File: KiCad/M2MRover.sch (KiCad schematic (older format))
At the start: 39 parts, among them J1 Light Detection, J10 MPU6050 Gyro & Acc GY-521, J11 microbit_edge_connector, J2 Serial (Bluetooth), J3 Servo, J4 H-Bridge, J5 Ultrasonic Down, J6 Ultrasonic Forward, J7 Compass GY-273, J8 Left Hall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

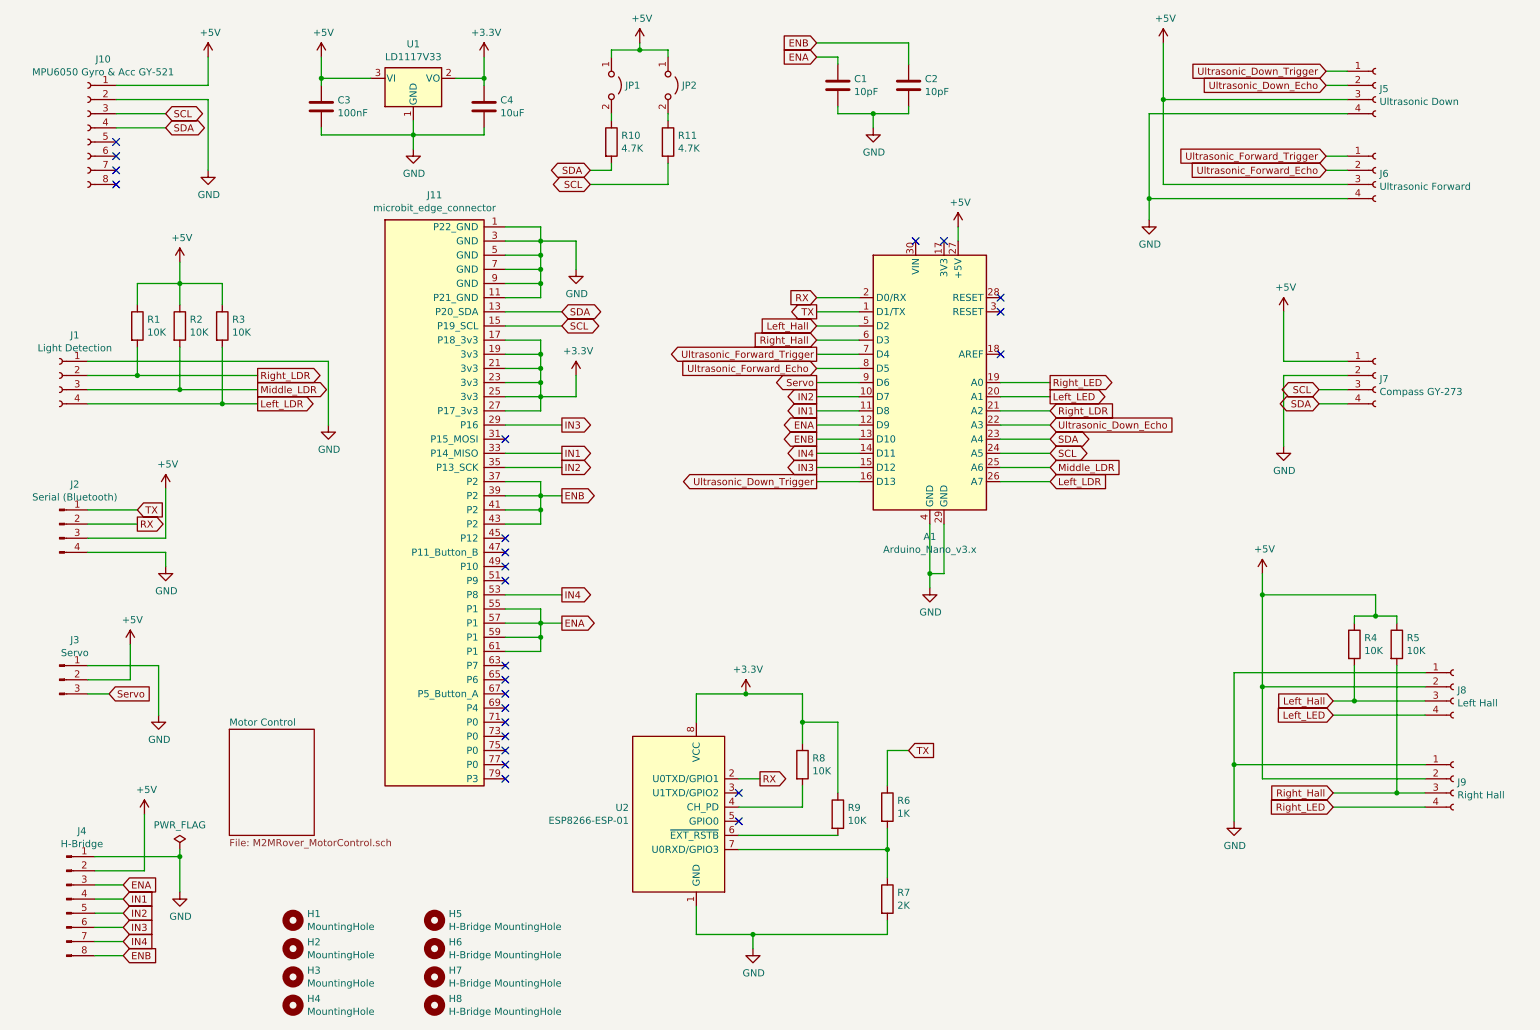
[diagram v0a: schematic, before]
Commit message: Add L298N H-Bridge driver
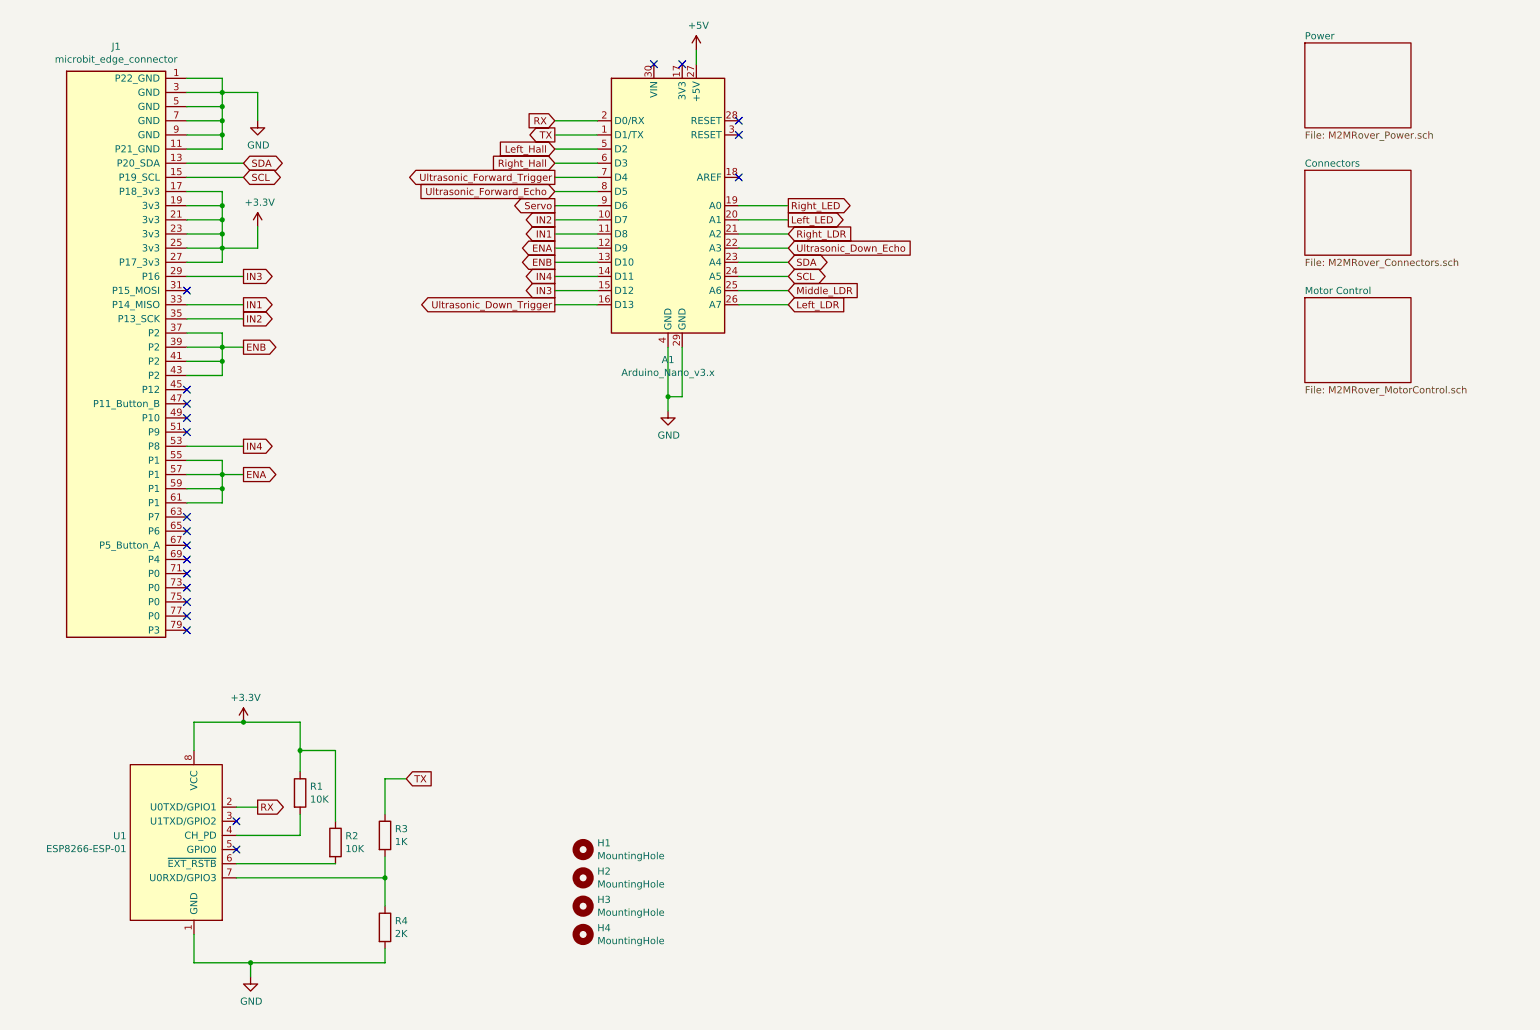
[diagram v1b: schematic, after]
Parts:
- removed C1, C2: 10pF, Capacitor_SMD:C_0805_2012Metric_Pad1.15x1.40mm_HandSolder, symbol Device:C
- removed C3: 100nF, Capacitor_SMD:C_0805_2012Metric_Pad1.15x1.40mm_HandSolder, symbol Device:C
- removed C4: 10uF, Capacitor_SMD:C_0805_2012Metric_Pad1.15x1.40mm_HandSolder, symbol Device:C
- removed H5, H6, H7, H8: H-Bridge MountingHole, MountingHole:MountingHole_2.7mm_Pad, symbol Mechanical:MountingHole
- removed J1: Light Detection, Connector_PinSocket_2.54mm:PinSocket_1x04_P2.54mm_Vertical, symbol Connector:Conn_01x04_Female
- removed J10: MPU6050 Gyro & Acc GY-521, Connector_PinSocket_2.54mm:PinSocket_1x08_P2.54mm_Vertical, symbol Connector:Conn_01x08_Female
- removed J2: Serial (Bluetooth), Connector_PinHeader_2.54mm:PinHeader_1x04_P2.54mm_Vertical, symbol Connector:Conn_01x04_Male
- removed J3: Servo, Connector_PinHeader_2.54mm:PinHeader_1x03_P2.54mm_Vertical, symbol Connector:Conn_01x03_Male
- removed J4: H-Bridge, Connector_PinHeader_2.54mm:PinHeader_1x08_P2.54mm_Vertical, symbol Connector:Conn_01x08_Male
- removed J5: Ultrasonic Down, Connector_PinSocket_2.54mm:PinSocket_1x04_P2.54mm_Vertical, symbol Connector:Conn_01x04_Female
- removed J6: Ultrasonic Forward, Connector_PinSocket_2.54mm:PinSocket_1x04_P2.54mm_Vertical, symbol Connector:Conn_01x04_Female
- removed J7: Compass GY-273, Connector_PinSocket_2.54mm:PinSocket_1x04_P2.54mm_Vertical, symbol Connector:Conn_01x04_Female
- removed J8: Left Hall, Connector_PinSocket_2.54mm:PinSocket_1x04_P2.54mm_Vertical, symbol Connector:Conn_01x04_Female
- removed J9: Right Hall, Connector_PinSocket_2.54mm:PinSocket_1x04_P2.54mm_Vertical, symbol Connector:Conn_01x04_Female
- removed JP1, JP2: Jumper_2_Open, Connector_PinHeader_2.54mm:PinHeader_1x02_P2.54mm_Vertical, symbol Jumper:Jumper_2_Open
- removed R1, R2, R3, R4, R5: 10K, Resistor_SMD:R_0805_2012Metric_Pad1.15x1.40mm_HandSolder, symbol Device:R
- removed R10, R11: 4.7K, Resistor_SMD:R_0805_2012Metric_Pad1.15x1.40mm_HandSolder, symbol Device:R
- removed U1: LD1117V33, Package_TO_SOT_THT:TO-220-3_Vertical, symbol Regulator_Linear:LD1117S33TR_SOT223
- renumbered J11 to J1, R8 to R1, R9 to R2, R6 to R3, R7 to R4, U2 to U1
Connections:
- no-connect marks 25 -> 21
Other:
- moved on the sheet: A1, H1, H2, H3, H4, J1, R1, R2, R3, R4, U1

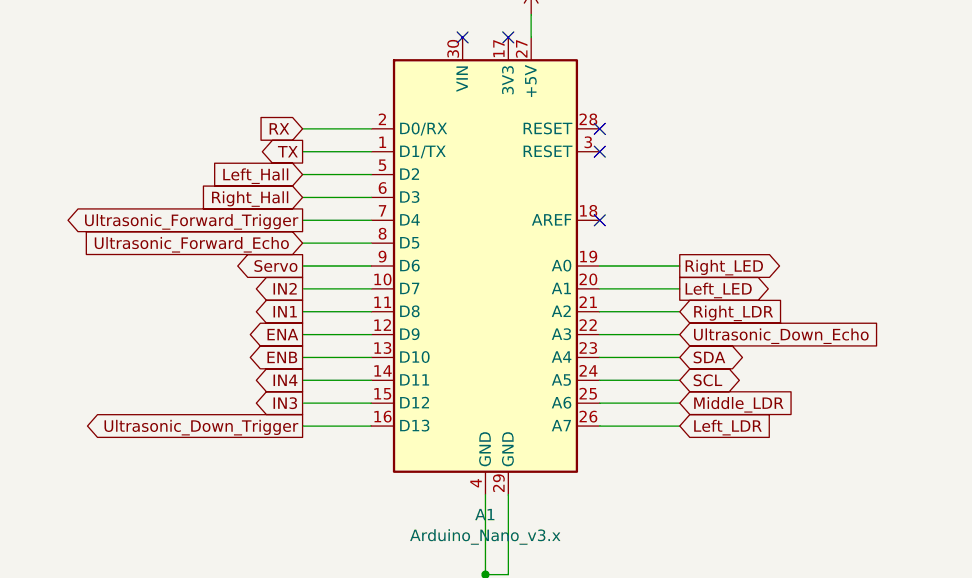
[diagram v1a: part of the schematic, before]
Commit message: Refactor motor wiring to h-bridge
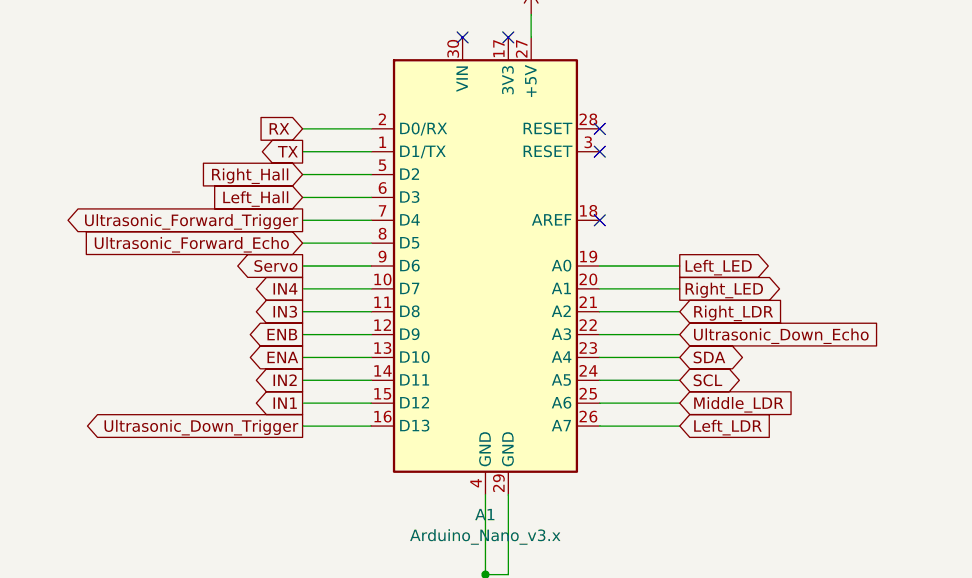
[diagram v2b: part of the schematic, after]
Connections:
- net ENA: now also A1.13 (D10); no longer A1.12 (D9)
- net ENB: now also A1.12 (D9); no longer A1.13 (D10)
- net IN1: now also A1.15 (D12); no longer A1.11 (D8)
- net IN2: now also A1.14 (D11); no longer A1.10 (D7)
- net IN3: now also A1.11 (D8); no longer A1.15 (D12)
- net IN4: now also A1.10 (D7); no longer A1.14 (D11)
- net Left_Hall: now also A1.6 (D3); no longer A1.5 (D2)
- net Left_LED: now also A1.19 (A0); no longer A1.20 (A1)
- net Right_Hall: now also A1.5 (D2); no longer A1.6 (D3)
- net Right_LED: now also A1.20 (A1); no longer A1.19 (A0)
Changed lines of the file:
@@
 	5350 850  5350 950
 Text GLabel 4350 2250 0    50   Output ~ 0
+ENB
+Text GLabel 4350 2150 0    50   Output ~ 0
+IN3
+Text GLabel 4350 2050 0    50   Output ~ 0
+IN4
+Text GLabel 4350 2550 0    50   Output ~ 0
+IN1
+Text GLabel 4350 2450 0    50   Output ~ 0
+IN2
+Text GLabel 4350 2350 0    50   Output ~ 0
 ENA
-Text GLabel 4350 2150 0    50   Output ~ 0
-IN1
-Text GLabel 4350 2050 0    50   Output ~ 0
-IN2
-Text GLabel 4350 2550 0    50   Output ~ 0
-IN3
-Text GLabel 4350 2450 0    50   Output ~ 0
-IN4
-Text GLabel 4350 2350 0    50   Output ~ 0
-ENB
 Wire Wire Line
 	4350 2550 4650 2550
@@
 	5650 2150 6000 2150
 Text GLabel 4350 1550 0    50   Input ~ 0
+Right_Hall
+Text GLabel 4350 1650 0    50   Input ~ 0
 Left_Hall
-Text GLabel 4350 1650 0    50   Input ~ 0
-Right_Hall
 Wire Wire Line
 	4350 1550 4650 1550
@@
 	4350 1850 4650 1850
 Text GLabel 6000 1950 2    50   Output ~ 0
+Left_LED
+Text GLabel 6000 2050 2    50   Output ~ 0
 Right_LED
-Text GLabel 6000 2050 2    50   Output ~ 0
-Left_LED
 Wire Wire Line
 	5650 2050 6000 2050
@@
 NoConn ~ 1750 4750
 NoConn ~ 1750 4850
-Wire Wire Line
-	1750 2450 2150 2450
-Wire Wire Line
-	1750 2650 2150 2650
-Wire Wire Line
-	1750 2750 2150 2750
-Wire Wire Line
-	2000 2950 2150 2950
-Wire Wire Line
-	1750 3650 2150 3650
-Wire Wire Line
-	2000 3850 2150 3850
 NoConn ~ 1750 2550
 $Comp
@@
 F1 "M2MRover_Connectors.sch" 50
 $EndSheet
+Wire Wire Line
+	1750 2450 2150 2450
+Wire Wire Line
+	1750 2650 2150 2650
+Wire Wire Line
+	1750 2750 2150 2750
+Wire Wire Line
+	2000 2950 2150 2950
+Wire Wire Line
+	1750 3650 2150 3650
+Wire Wire Line
+	2000 3850 2150 3850
 $EndSCHEMATC

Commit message: Route the PCB
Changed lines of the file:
@@
 	1750 2450 2150 2450
 Wire Wire Line
-	1750 2650 2150 2650
+	2150 2650 1750 2650
 Wire Wire Line
 	1750 2750 2150 2750
 Wire Wire Line
-	2000 2950 2150 2950
+	2150 2950 2000 2950
 Wire Wire Line
-	1750 3650 2150 3650
+	2150 3650 1750 3650
 Wire Wire Line
-	2000 3850 2150 3850
+	2150 3850 2000 3850
 $EndSCHEMATC

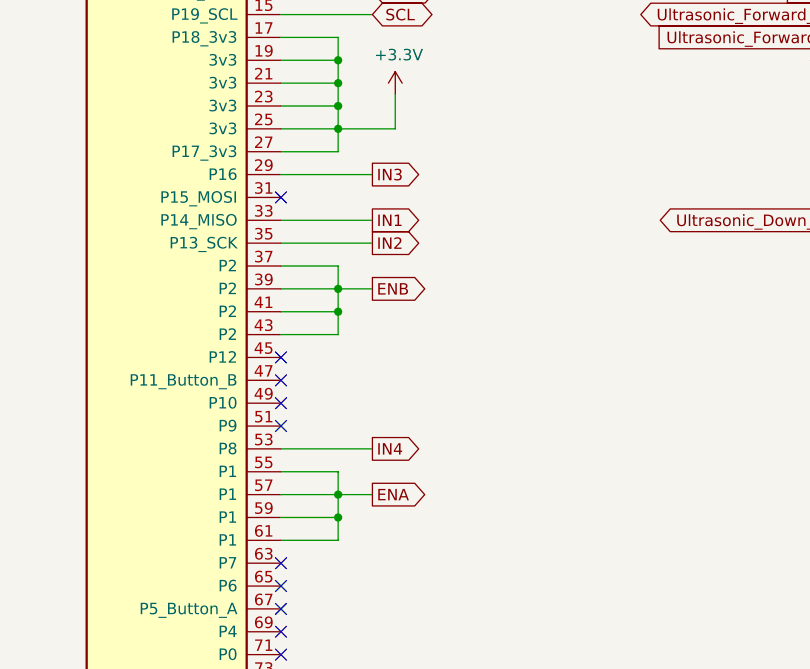
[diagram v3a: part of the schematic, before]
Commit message: Track all remaining of components
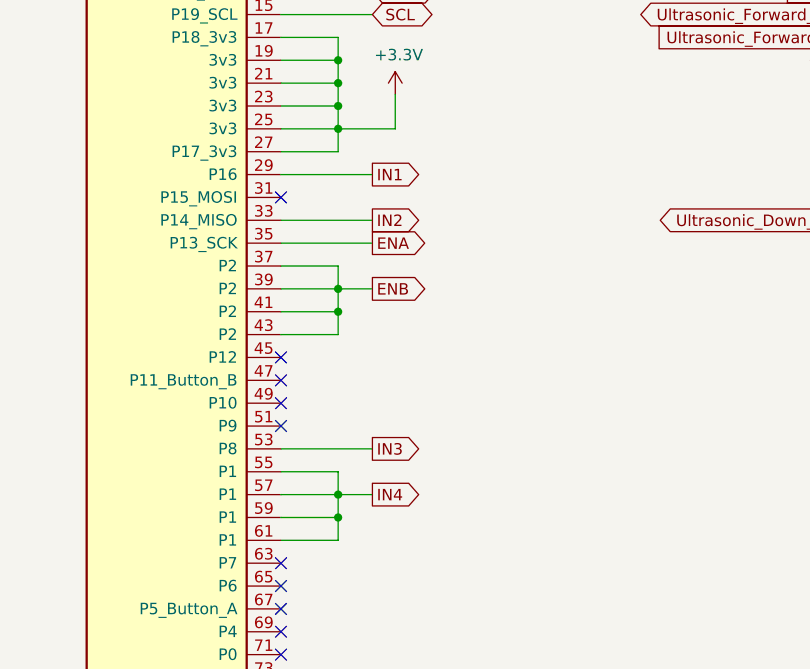
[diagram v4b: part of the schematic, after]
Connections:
- net ENA: now also J1.35 (P13_SCK); no longer J1.55 (P1), J1.57 (P1), J1.59 (P1), J1.61 (P1)
- net IN1: now also J1.29 (P16); no longer J1.33 (P14_MISO)
- net IN2: now also J1.33 (P14_MISO); no longer J1.35 (P13_SCK)
- net IN3: now also J1.53 (P8); no longer J1.29 (P16)
- net IN4: now also J1.55 (P1), J1.57 (P1), J1.59 (P1), J1.61 (P1); no longer J1.53 (P8)
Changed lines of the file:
@@
 	2250 2250 2000 2250
 Text GLabel 2150 2650 2    50   Output ~ 0
+IN2
+Text GLabel 2150 2750 2    50   Output ~ 0
+ENA
+Text GLabel 2150 2450 2    50   Output ~ 0
 IN1
-Text GLabel 2150 2750 2    50   Output ~ 0
-IN2
-Text GLabel 2150 2450 2    50   Output ~ 0
+Text GLabel 2150 3650 2    50   Output ~ 0
 IN3
-Text GLabel 2150 3650 2    50   Output ~ 0
+Text GLabel 2150 3850 2    50   Output ~ 0
 IN4
-Text GLabel 2150 3850 2    50   Output ~ 0
-ENA
 Text GLabel 2150 2950 2    50   Output ~ 0
 ENB

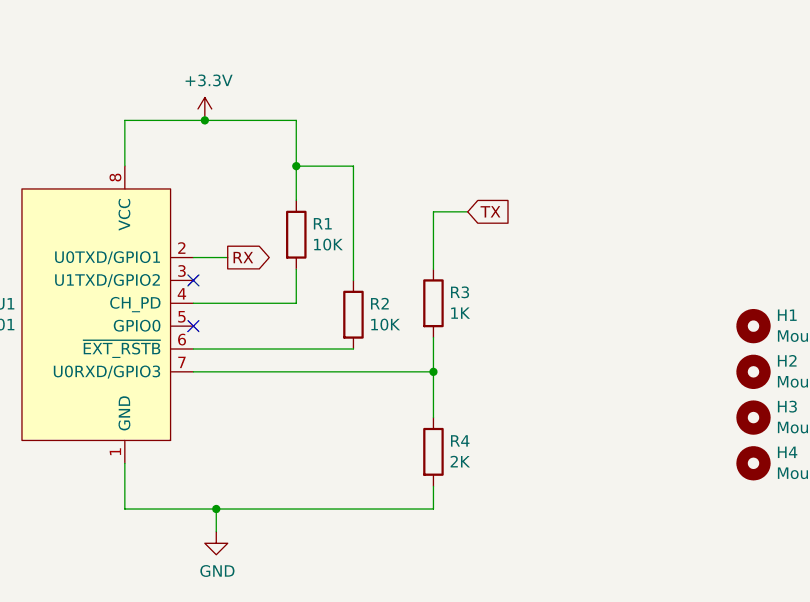
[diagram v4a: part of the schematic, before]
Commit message: Add pull up resistor to ESP8266 GPIO0 and remove GND tracks
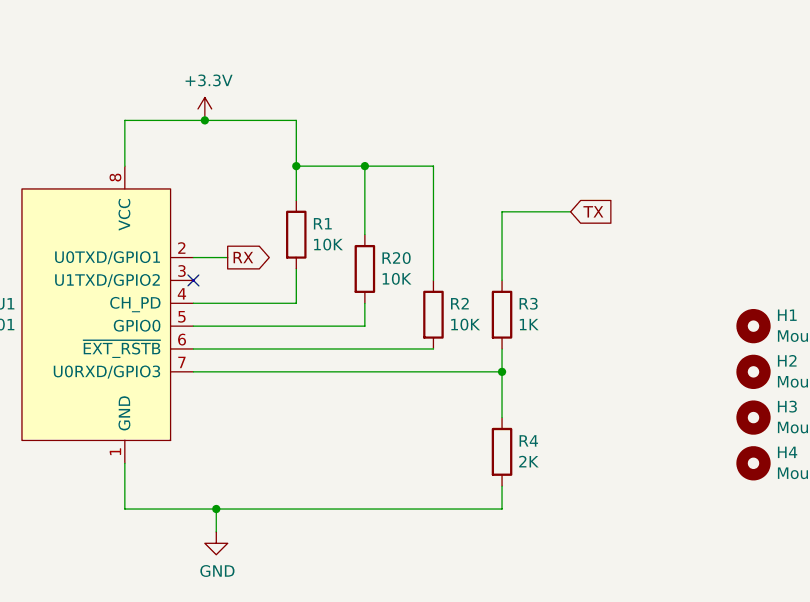
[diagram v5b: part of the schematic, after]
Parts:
- added R20: 10K, Resistor_SMD:R_0805_2012Metric_Pad1.15x1.40mm_HandSolder, symbol Device:R
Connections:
- net +3V3: now also R20.1
- net at U1.5 (GPIO0): now also R20.2
- no-connect marks 21 -> 20
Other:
- moved on the sheet: R2, R3, R4
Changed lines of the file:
@@
 L Device:R R2
 U 1 1 5D69B79B
-P 2800 6450
-F 0 "R2" H 2870 6496 50  0000 L CNN
-F 1 "10K" H 2870 6405 50  0000 L CNN
-F 2 "Resistor_SMD:R_0805_2012Metric_Pad1.15x1.40mm_HandSolder" V 2730 6450 50  0001 C CNN
-F 3 "~" H 2800 6450 50  0001 C CNN
-	1    2800 6450
+P 3150 6450
+F 0 "R2" H 3220 6496 50  0000 L CNN
+F 1 "10K" H 3220 6405 50  0000 L CNN
+F 2 "Resistor_SMD:R_0805_2012Metric_Pad1.15x1.40mm_HandSolder" V 3080 6450 50  0001 C CNN
+F 3 "~" H 3150 6450 50  0001 C CNN
+	1    3150 6450
 	1    0    0    -1
 $EndComp
@@
 	2550 5950 2550 5800
 Wire Wire Line
-	2550 5800 2800 5800
+	2550 5800 2850 5800
 Wire Wire Line
-	2800 5800 2800 6300
+	3150 5800 3150 6300
 Wire Wire Line
-	2100 6600 2800 6600
+	2100 6600 3150 6600
 $Comp
 L Device:R R3
 U 1 1 5D776F56
-P 3150 6400
-F 0 "R3" H 3220 6446 50  0000 L CNN
-F 1 "1K" H 3220 6355 50  0000 L CNN
-F 2 "Resistor_SMD:R_0805_2012Metric_Pad1.15x1.40mm_HandSolder" V 3080 6400 50  0001 C CNN
-F 3 "~" H 3150 6400 50  0001 C CNN
-	1    3150 6400
+P 3450 6450
+F 0 "R3" H 3520 6496 50  0000 L CNN
+F 1 "1K" H 3520 6405 50  0000 L CNN
+F 2 "Resistor_SMD:R_0805_2012Metric_Pad1.15x1.40mm_HandSolder" V 3380 6450 50  0001 C CNN
+F 3 "~" H 3450 6450 50  0001 C CNN
+	1    3450 6450
 	1    0    0    -1
 $EndComp
@@
 L Device:R R4
 U 1 1 5D777435
-P 3150 7050
-F 0 "R4" H 3220 7096 50  0000 L CNN
-F 1 "2K" H 3220 7005 50  0000 L CNN
-F 2 "Resistor_SMD:R_0805_2012Metric_Pad1.15x1.40mm_HandSolder" V 3080 7050 50  0001 C CNN
-F 3 "~" H 3150 7050 50  0001 C CNN
-	1    3150 7050
+P 3450 7050
+F 0 "R4" H 3520 7096 50  0000 L CNN
+F 1 "2K" H 3520 7005 50  0000 L CNN
+F 2 "Resistor_SMD:R_0805_2012Metric_Pad1.15x1.40mm_HandSolder" V 3380 7050 50  0001 C CNN
+F 3 "~" H 3450 7050 50  0001 C CNN
+	1    3450 7050
 	1    0    0    -1
 $EndComp
-Text GLabel 3300 6000 2    50   Input ~ 0
+Text GLabel 3750 6000 2    50   Input ~ 0
 TX
 Wire Wire Line
-	3150 6000 3150 6250
+	3450 6000 3450 6300
 Wire Wire Line
-	3150 7200 3150 7300
+	3450 7200 3450 7300
 Wire Wire Line
-	3150 6550 3150 6700
+	3450 6600 3450 6700
 Wire Wire Line
-	2100 6700 3150 6700
-Connection ~ 3150 6700
+	2100 6700 3450 6700
+Connection ~ 3450 6700
 Wire Wire Line
-	3150 6700 3150 6900
+	3450 6700 3450 6900
 Text GLabel 2250 6200 2    50   Output ~ 0
 RX
@@
 Connection ~ 2550 5800
 Wire Wire Line
-	3150 6000 3300 6000
+	3450 6000 3750 6000
 Wire Wire Line
-	3150 7300 2200 7300
+	3450 7300 2200 7300
 Wire Wire Line
 	2200 7400 2200 7300
@@
 	2200 7300 1800 7300
 NoConn ~ 2100 6300
-NoConn ~ 2100 6500
 Wire Wire Line
 	2100 6400 2550 6400
@@
 Wire Wire Line
 	2150 3850 2000 3850
+$Comp
+L Device:R R20
+U 1 1 5D9393D6
+P 2850 6250
+F 0 "R20" H 2920 6296 50  0000 L CNN
+F 1 "10K" H 2920 6205 50  0000 L CNN
+F 2 "Resistor_SMD:R_0805_2012Metric_Pad1.15x1.40mm_HandSolder" V 2780 6250 50  0001 C CNN
+F 3 "~" H 2850 6250 50  0001 C CNN
+	1    2850 6250
+	1    0    0    -1
+$EndComp
+Wire Wire Line
+	2100 6500 2850 6500
+Wire Wire Line
+	2850 6500 2850 6400
+Wire Wire Line
+	2850 6100 2850 5800
+Connection ~ 2850 5800
+Wire Wire Line
+	2850 5800 3150 5800
 $EndSCHEMATC
